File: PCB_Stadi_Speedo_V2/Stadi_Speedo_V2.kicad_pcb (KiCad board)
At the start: 4 copper layers, 41.7 x 44 mm, 80 parts, among them J2 OLED I2C, J3 ICSP, J4 OLED SH1106, J5 SPÍD & PWR, J6 AUX DDAA, J7 ENG RPM, U1 Mikroprofesor, U3 LM1117MP-5.0, U4 ME6211C33M5, U5 MAX31855KASA, Y1 16MHz

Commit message: Upravy Routingu
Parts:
- turned R11 to -90 degrees
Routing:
- net +3V3: track 40.8 -> 36.9 mm
- net /D8/SO K: track 17.1 -> 14.4 mm, vias 2 -> 3
- net /D2_SPD: track 19.5 -> 17.7 mm
- net GND: vias 119 -> 120

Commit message: BUCK KONVERTER ADD
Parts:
- removed the ? at (123.7, 157.3)
- removed U3: LM1117MP-5.0, Package_TO_SOT_SMD:SOT-223-3_TabPin2
- added C35: 100n, Capacitor_SMD:C_0603_1608Metric, F.Cu at (136.5, 172.2)
- added C36: 100n, Capacitor_SMD:C_0603_1608Metric, F.Cu at (136.5, 174.7)
- added L1: L_Ferrite, Inductor_SMD:L_Bourns_SRP2313AA, F.Cu at (111.2, 147.9)
- added R24: 100k, Resistor_SMD:R_0603_1608Metric, F.Cu at (136.5, 177.2)
- added R25: 19.1k, Resistor_SMD:R_0603_1608Metric, F.Cu at (136.5, 179.7)
- added U6: LMR51610YDBVR, Package_TO_SOT_SMD:SOT-23-6, F.Cu at (116.2, 154.4)
- C5: value 1u -> 4u7
- moved R5 1.94 mm to (126.0, 153.1)
- moved C5 1.85 mm to (120.9, 154.0)
- moved D3 1.80 mm to (120.9, 159.2)
- moved D9 1.80 mm to (120.9, 157.2)
- moved FB5 0.63 mm to (124.3, 156.8)
- renumbered OPT0 to Q1, OPTO to Q2
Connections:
- R23 pad 1: /T+ -> Net-(U5-~{CS})
- R23 pad 2: /T- -> /D6/CS K
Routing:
- net +5V: track 81.7 -> 57.0 mm
- net Net-(D9-K): track 11.9 -> 7.57 mm
- net GND: track 19.2 -> 16.8 mm, vias 120 -> 116
- net VCC: track 3.40 -> 2.21 mm
- net Net-(D2-A): track 8.43 -> 7.85 mm
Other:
- board text added: "OPTO"
- board text removed: "Q1"
- board text removed: "Q2"

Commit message: Naroutovany DCDC
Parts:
- added C32: 100n, Capacitor_SMD:C_0603_1608Metric, B.Cu at (107.5, 150.6)
- added C33: 1u, Capacitor_SMD:C_0603_1608Metric, B.Cu at (106.2, 152.1)
- added C34: 100n, Capacitor_SMD:C_0603_1608Metric, B.Cu at (110.6, 150.1)
- added C37: 4u7_16V, Capacitor_Tantalum_SMD:CP_EIA-3216-10_Kemet-I, F.Cu at (105.5, 145.8)
- added TP3: Label, TestPoint:TestPoint_Pad_D1.5mm, F.Cu at (113.5, 135.3)
- added TP4: Label, TestPoint:TestPoint_Pad_D1.5mm, F.Cu at (116.3, 135.2)
- added TP5: Label, TestPoint:TestPoint_Pad_D1.0mm, F.Cu at (115.7, 140.8)
- added TP6: Label, TestPoint:TestPoint_Pad_D1.0mm, F.Cu at (113.8, 141.5)
- C35: value 100n -> 4u7_16V; footprint Capacitor_SMD:C_0603_1608Metric -> AERO_Capacitor_SMD:C_0603-1206_universal_Pad1.18x1.45mm
- C5: footprint Capacitor_SMD:C_0603_1608Metric -> AERO_Capacitor_SMD:C_0603-1206_universal_Pad1.18x1.45mm
- D3, D9: footprint Diode_SMD:D_SOD-123F -> AERO_Diode_SMD:D_SOD-123FL
- FB5: footprint Inductor_SMD:L_Pulse_PA4332 -> AERO_Capacitor_SMD:C_0603-1206_universal_Pad1.18x1.45mm
- FB6: footprint Inductor_SMD:L_Pulse_PA4332 -> AERO_Capacitor_SMD:C_0603-1206_universal_Pad1.33x1.80mm_HandSolder
- R10, R12: moved to B.Cu
- moved R25 30.3 mm to (114.5, 158.8)
- moved C36 28.8 mm to (115.0, 155.5), turned to 90 degrees
- moved C35 28.5 mm to (116.6, 151.8)
- moved R24 26.3 mm to (117.6, 158.8)
- moved R23 7.92 mm to (114.8, 144.4), turned to -90 degrees
- moved U6 1.44 mm to (117.5, 155.0)
- moved FB5 1.41 mm to (125.7, 156.6)
- moved D9 1.24 mm to (121.9, 156.5)
- moved R12 1.02 mm to (111.2, 158.8)
- moved C5 0.98 mm to (121.9, 154.0)
- moved R10 0.92 mm to (114.3, 158.8)
- moved D3 0.92 mm to (121.8, 159.0)
- moved ? 0.73 mm to (105.7, 149.1)
- moved C14 0.62 mm to (115.5, 138.5)
- moved R1 0.62 mm to (114.0, 138.5)
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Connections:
- net Net-(U6-SW) renamed /sw
- C35 pad 1: Net-(D9-K) -> +5V
- U1 pad 25: unconnected-(U1-PC2-Pad25) -> Net-(U1-PC2)
- U1 pad 26: unconnected-(U1-PC3-Pad26) -> Net-(U1-PC3)
- U1 pad 30: Net-(U1-PD0) -> /PD0
- U1 pad 31: Net-(U1-PD1) -> /PD1
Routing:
- net +5V: track 57.0 -> 68.0 mm, vias 10 -> 15
- net Net-(U1-PC3): track 0.00 -> 10.2 mm
- net Net-(U1-PC2): track 0.00 -> 8.57 mm
- net /D13/SCK_: track 38.0 -> 30.4 mm
- net Net-(U6-FB): track 0.00 -> 4.81 mm
- net Net-(U5-~{CS}): track 5.31 -> 10.1 mm
- net /D6/CS K: track 17.2 -> 20.5 mm
- net /PD1: track 0.00 -> 2.82 mm
- net GND: track 16.8 -> 19.3 mm, vias 116 -> 127
- net Net-(D9-K): track 7.57 -> 9.76 mm
- net /RESET_: track 19.5 -> 21.6 mm
- net /PD0: track 0.00 -> 1.76 mm
- net Net-(U6-CB): track 0.00 -> 1.61 mm
- net +3V3: track 36.9 -> 38.3 mm
- net Net-(D8-A2): track 22.3 -> 20.9 mm
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- added copper zone on B.Cu, net +3V3
- added copper zone on F.Cu, net /sw

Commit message: drobná škatulátka
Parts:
- moved R10 3.49 mm to (115.0, 155.4), turned to 35 degrees
- moved R12 1.56 mm to (112.2, 157.6), turned to -143 degrees
- moved ? 1.07 mm to (106.7, 148.7), turned to -135 degrees
- moved FB6 0.25 mm to (119.1, 156.6)
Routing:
- net /D2_SPD: track 18.5 -> 21.1 mm
- net Net-(D7-K): track 2.69 -> 3.91 mm
- net +3V3: track 38.3 -> 37.5 mm
- net +5V: track 68.0 -> 68.7 mm
- net GND: vias 127 -> 126

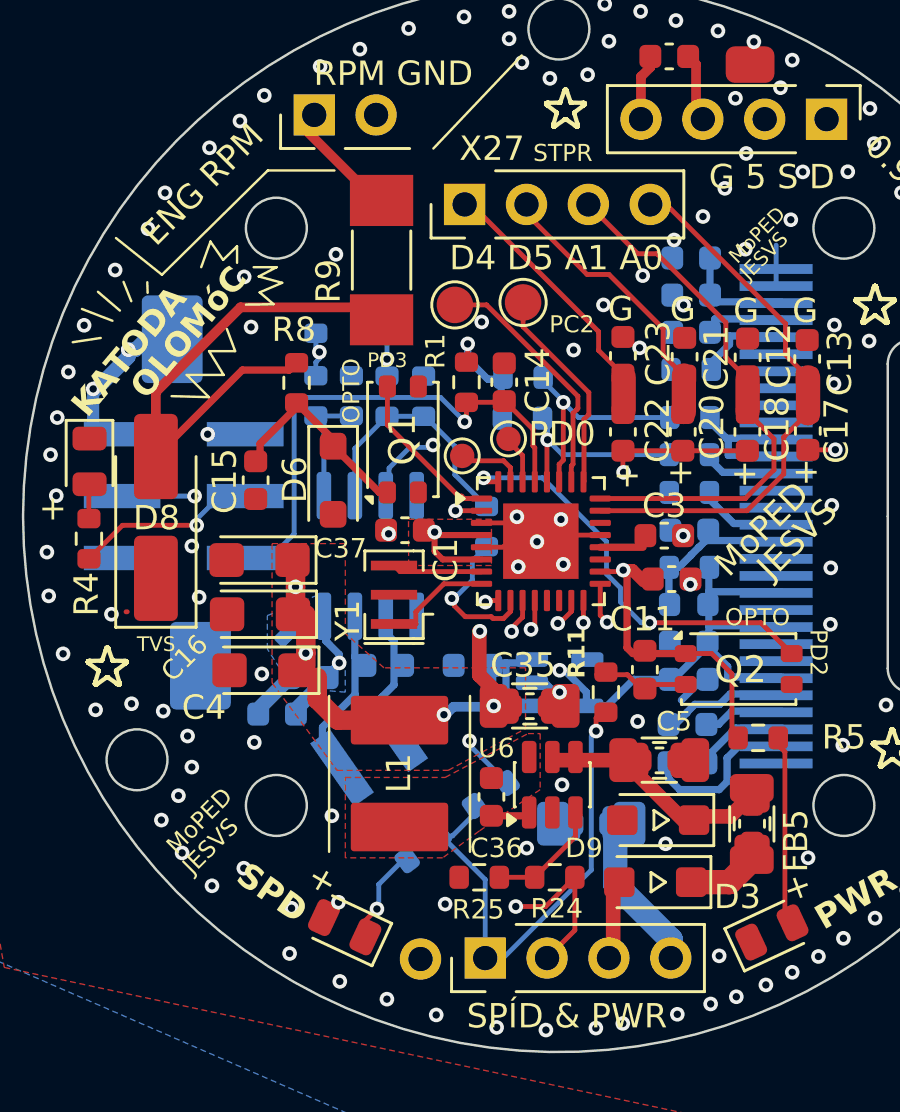
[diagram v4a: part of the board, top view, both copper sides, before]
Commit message: pridany ferity na termistor a 5V
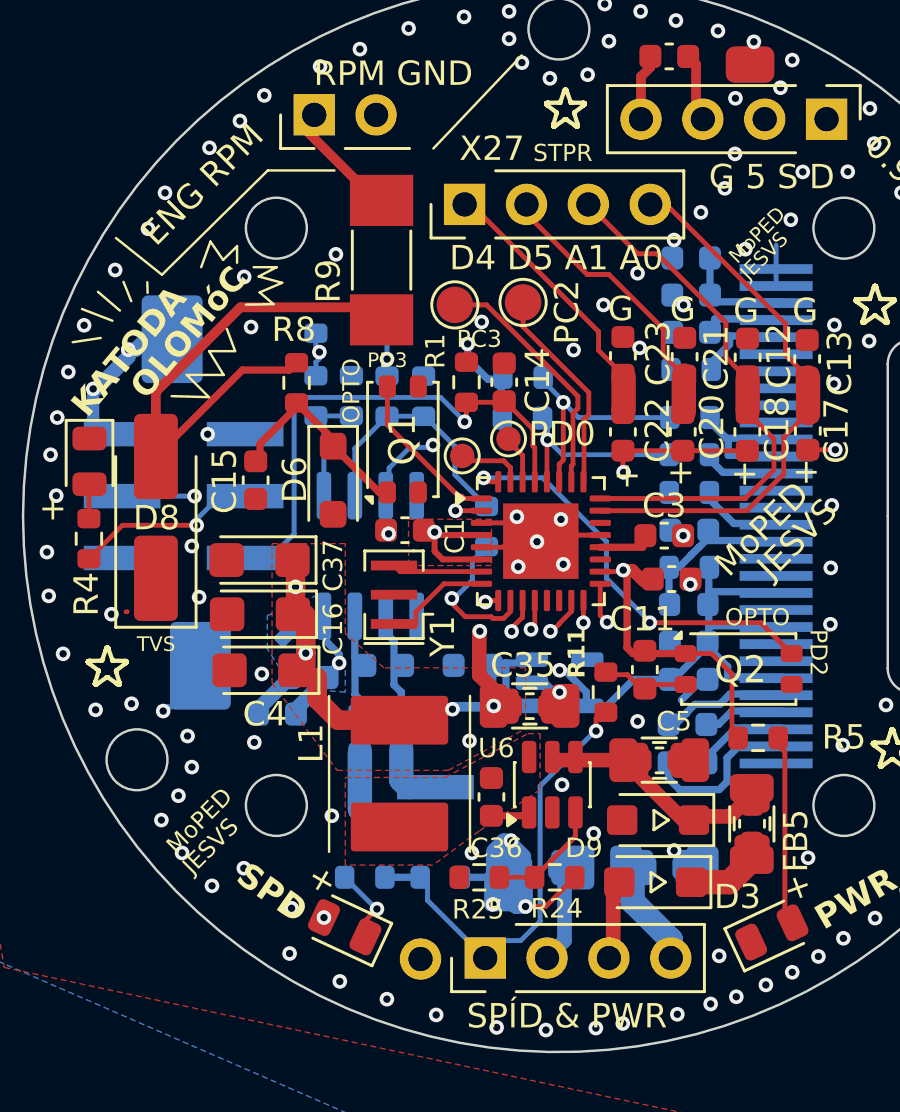
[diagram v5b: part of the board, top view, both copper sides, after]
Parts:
- added FB1: FerriteBead_Small, Inductor_SMD:L_0603_1608Metric, B.Cu at (109.6, 152.9)
- added FB2: FerriteBead_Small, Inductor_SMD:L_0603_1608Metric, B.Cu at (111.3, 152.8)
- added FB7: FerriteBead_4A_180Ω, AERO_Capacitor_SMD:C_0603-1206_universal_Pad1.33x1.80mm_HandSolder, B.Cu at (117.0, 158.4)
- moved R10 3.98 mm to (112.9, 158.8), turned to 0 degrees
- moved ? 3.55 mm to (111.4, 156.8), turned to 180 degrees
- moved FB6 3.50 mm to (122.1, 158.4), turned to 180 degrees
- moved ? 2.72 mm to (112.7, 155.1), turned to 0 degrees
- moved R12 2.68 mm to (109.8, 158.8), turned to 180 degrees
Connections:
- C34 pad 1: /T- -> Net-(U5-T-)
- C34 pad 2: /T+ -> Net-(U5-T+)
- J5 pad 2: +5V -> Net-(J5-Pin_2)
- U5 pad 2: /T- -> Net-(U5-T-)
- U5 pad 3: /T+ -> Net-(U5-T+)
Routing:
- net +5V: track 68.7 -> 75.4 mm, vias 15 -> 17
- net Net-(U5-T-): track 0.00 -> 4.19 mm
- net Net-(U5-T+): track 0.00 -> 4.12 mm
- net Net-(J5-Pin_2): track 0.00 -> 4.03 mm
- net /T-: track 5.42 -> 2.74 mm
- net /T+: track 7.11 -> 4.44 mm
- net /D2_SPD: track 21.1 -> 19.1 mm
- net Net-(J5-Pin_4): track 6.21 -> 4.33 mm
- net GND: track 19.3 -> 20.1 mm
- net Net-(D7-K): track 3.91 -> 3.23 mm
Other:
- board text added: "T+"
- board text added: "T-"
- board text removed: "T- T+"
